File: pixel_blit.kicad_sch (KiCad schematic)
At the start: 42 parts, among them J37 Conn_01x03_Pin, SW1 K2-1808SN-A4SW, U1 RP2350B_C42415655, U10 APS6404L-3SQR-SN, U2 W25Q128JVSIQTR

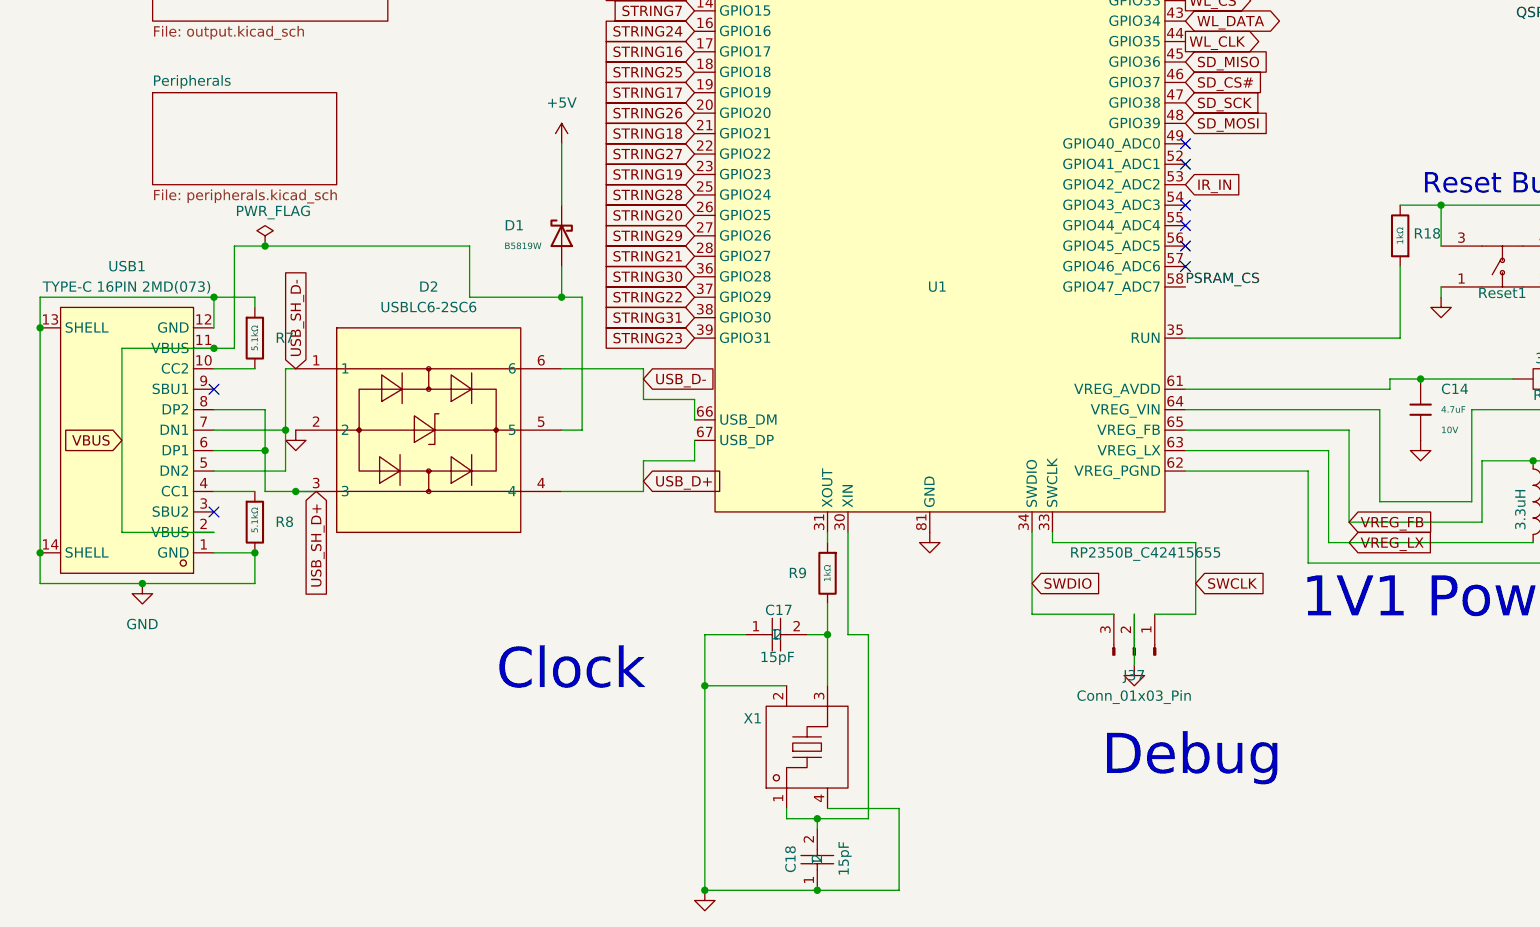
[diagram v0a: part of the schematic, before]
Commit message: Add status RGB LED, user button and blown-fuse LEDs
- D14 common-cathode RGB (C601684) with R72-R74 on GPIO 41/44/45, SW3
  'Play' on GPIO 43; routed from U1 via short F.Cu escapes and In2 lanes
  to the old display area. GPIO 40 and 46 stay spare.
- D15-D18 red LEDs with 10k 0603 across each zone fuse, between holder
  and input terminal.
- Zone borders regenerated; plan doc GPIO map updated.
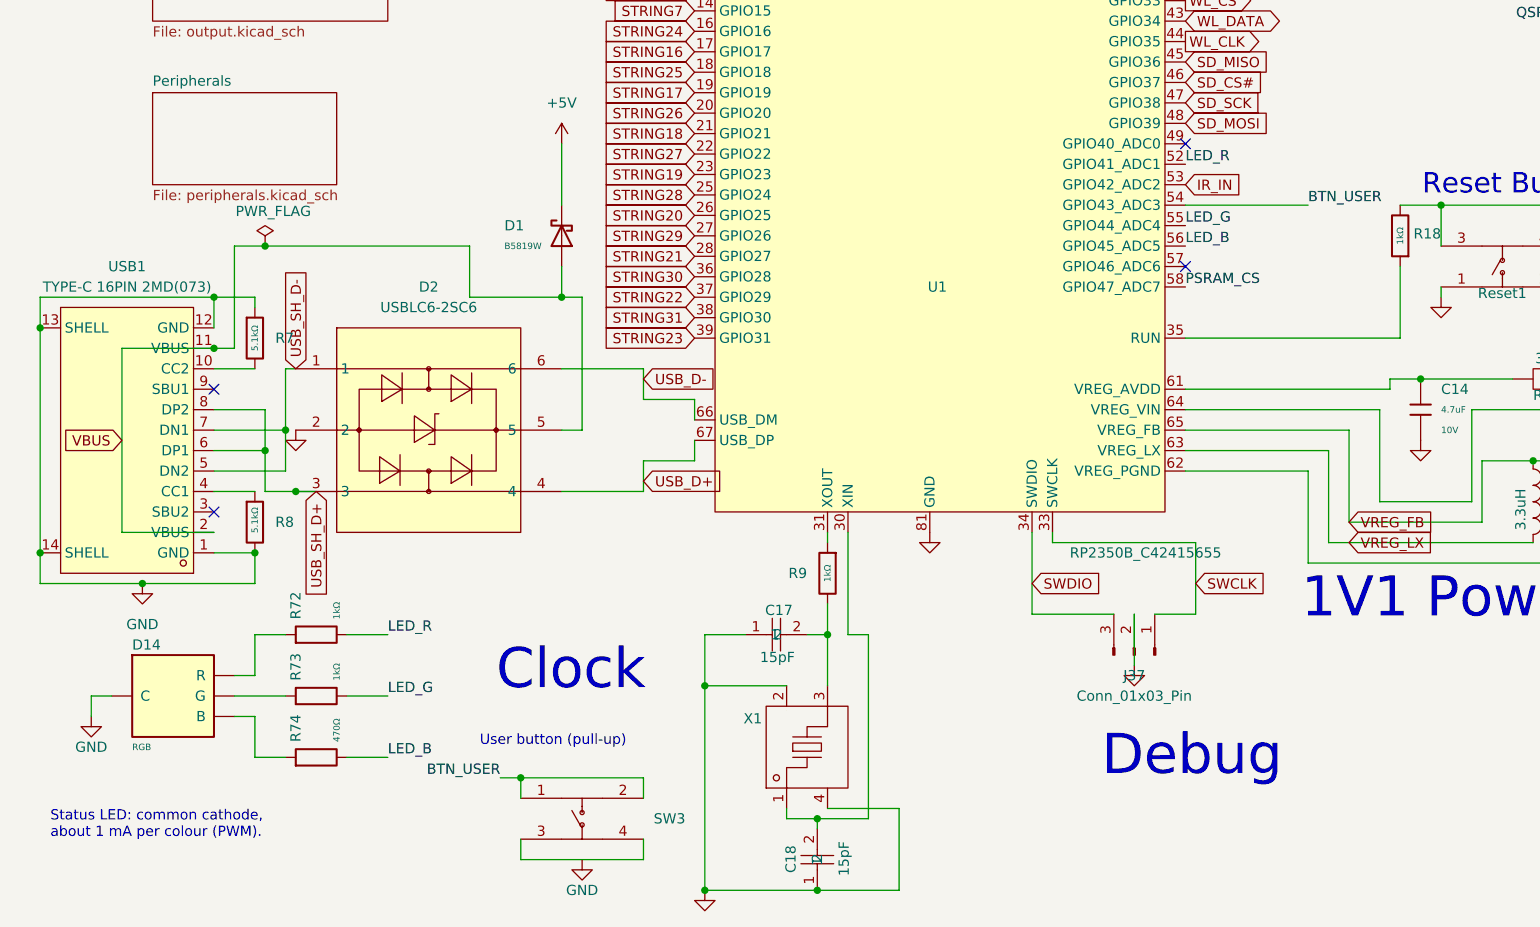
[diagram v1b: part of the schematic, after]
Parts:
- added D14: RGB, JLCImport:TJ-S1615CY6TGLCCSRGB-A5, symbol JLCImport:TJ-S1615CY6TGLCCSRGB-A5
- added R72, R73: 1kΩ, PixelBlit:R_0402, symbol PixelBlit:0402,1kΩ
- added R74: 470Ω, PixelBlit:R_0402, symbol PixelBlit:0402,470Ω
- added SW3: (no value), PixelBlit:KEY-SMD_4P-L4.2-W3.2-P2.20-LS5.1-TL, symbol PixelBlit:K2-1808SN-A4SW
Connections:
- net GND: now also D14.1 (C), SW3.3, SW3.4
- net LED_R: now reaches U1.52 (GPIO41_ADC1)
- net LED_R: now also R72.2
- net BTN_USER: now reaches U1.54 (GPIO43_ADC3)
- net BTN_USER: now also SW3.1, SW3.2
- net LED_G: now reaches U1.55 (GPIO44_ADC4)
- net LED_G: now also R73.2
- net LED_B: now reaches U1.56 (GPIO45_ADC5)
- net LED_B: now also R74.2
- new net: D14.3 (G), R73.1
- new net: D14.2 (B), R74.1
- new net: D14.4 (R), R72.1
- no-connect marks 8 -> 4
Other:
- note added: "Status LED: common cathode, about 1 mA per colour (PWM)."
- note added: "User button (pull-up)"

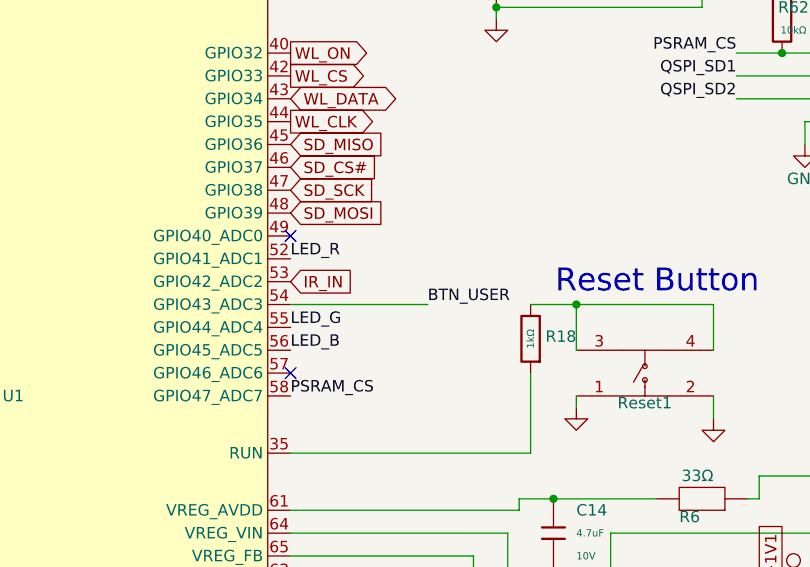
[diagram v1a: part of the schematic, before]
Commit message: Route status LED and button on the old display-panel lines
Replace the In2 lanes with the old TRB/TRA/PSH routes (red GPIO 43,
green GPIO 45, blue GPIO 41) and restore BAK (GPIO 40) for the Play
button. PSH's B.Cu tail moves to F.Cu beside TRB with a short hop under
IR_IN; Boot moves right to clear TRA; RUN via shifted 1 mm.
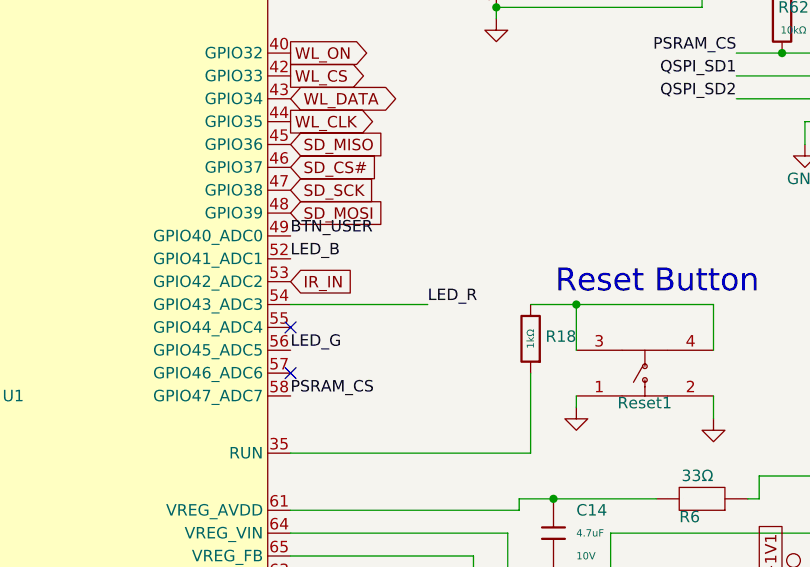
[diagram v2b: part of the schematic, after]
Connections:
- net BTN_USER: now also U1.49 (GPIO40_ADC0); no longer U1.54 (GPIO43_ADC3)
- net LED_B: now also U1.52 (GPIO41_ADC1); no longer U1.56 (GPIO45_ADC5)
- net LED_G: now also U1.56 (GPIO45_ADC5); no longer U1.55 (GPIO44_ADC4)
- net LED_R: now also U1.54 (GPIO43_ADC3); no longer U1.52 (GPIO41_ADC1)

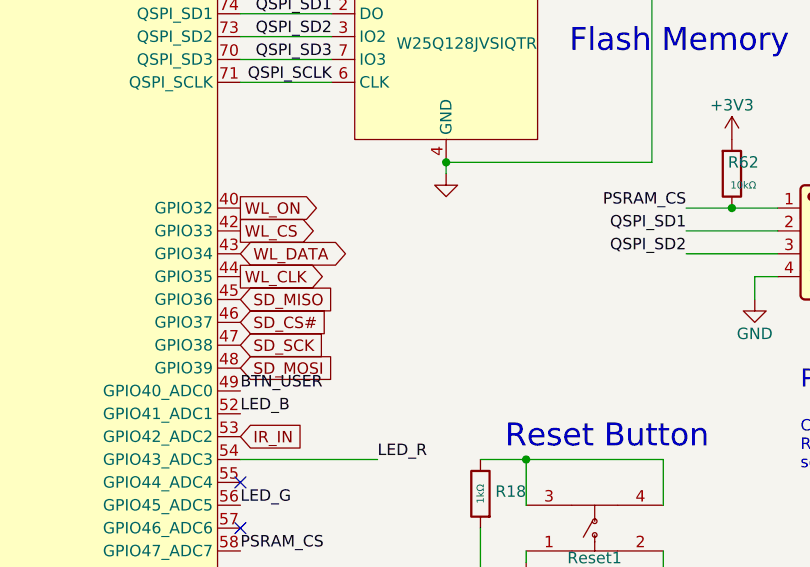
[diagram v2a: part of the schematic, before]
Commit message: Reroute Wi-Fi lanes off SD_MOSI, add 33 ohm series resistor R75 on WL_CLK
The user's In2 reroute shortens the RM2 SPI lines from 147-173 mm to 70-85 mm.
Audit item 2 marked done; README resistor count updated.
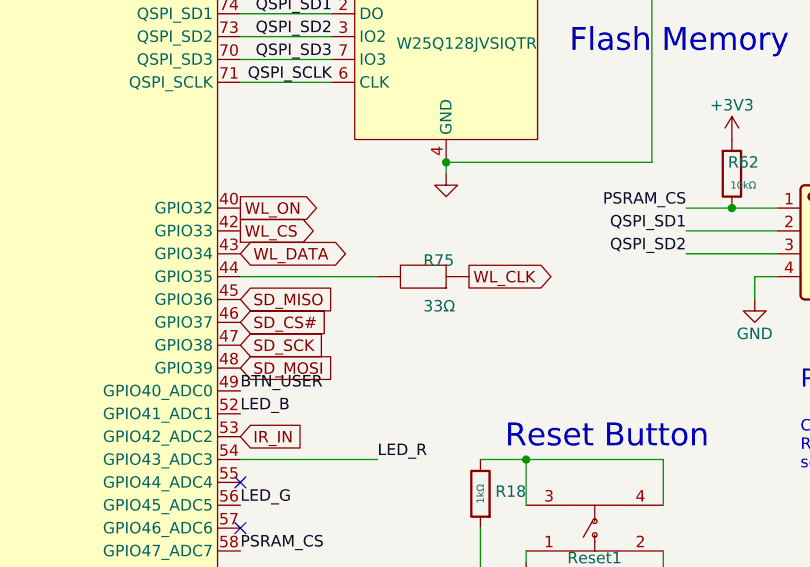
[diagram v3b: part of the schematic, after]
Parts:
- added R75: 33Ω, PixelBlit:R0402, symbol PixelBlit:RT0402BRD0733RL
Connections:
- net WL_CLK: now also R75.1; no longer U1.44 (GPIO35)
- new net: R75.2, U1.44 (GPIO35)
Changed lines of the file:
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@@
 		)
 	)
+	(wire
+		(pts
+			(xy 156.21 88.9) (xy 171.45 88.9)
+		)
+		(stroke
+			(width 0)
+			(type default)
+		)
+	)
 	(global_label "WL_CLK"
 		(shape output)
-		(at 156.21 88.9 0)
+		(at 181.61 88.9 0)
 		(fields_autoplaced yes)
 		(effects
@@
 		)
 		(property "Intersheetrefs" "${INTERSHEET_REFS}"
-			(at 168.3271 88.9 0)
+			(at 193.7271 88.9 0)
 			(hide yes)
 			(show_name no)
@@
 					(unit 1)
 				)
+			)
+		)
+	)
+	(symbol
+		(lib_id "PixelBlit:RT0402BRD0733RL")
+		(at 176.53 88.9 0)
+		(mirror y)
+		(unit 1)
+		(body_style 1)
+		(exclude_from_sim no)
+		(in_bom yes)
+		(on_board yes)
+		(in_pos_files yes)
+		(dnp no)
+		(property "Reference" "R75"
+			(at 176.53 86.36 0)
+			(show_name no)
+			(do_not_autoplace no)
+			(effects
+				(font
+					(size 1.27 1.27)
+				)
+				(justify right top)
+			)
+		)
+		(property "Value" "33Ω"
+			(at 176.53 91.44 0)
+			(show_name no)
+			(do_not_autoplace no)
+			(effects
+				(font
+					(size 1.27 1.27)
+				)
+				(justify right top)
+			)
+		)
+		(property "Footprint" "PixelBlit:R0402"
+			(at 176.53 88.9 0)
+			(hide yes)
+			(show_name no)
+			(do_not_autoplace no)
+			(effects
+				(font
+					(size 1.27 1.27)
+				)
+			)
+		)
+		(property "Datasheet" "https://atta.szlcsc.com/upload/public/pdf/source/20200306/C422600_1E6D84923E4A46A82E41ADD87F860B5C.pdf"
+			(at 176.53 88.9 0)
+			(hide yes)
+			(show_name no)
+			(do_not_autoplace no)
+			(effects
+				(font
+					(size 1.27 1.27)
+				)
+			)
+		)
+		(property "Description" "Type:Thick Film Resistors Resistance:33Ω Tolerance:±1% Tolerance:±1% Power(Watts): Overload Voltage (Max): Temperature Coefficient:±100ppm/℃ Temperature Coefficient:±100ppm/℃ Operating Temperature Range:-55℃~+155℃ Operating Temperature Range:-55℃~+155℃"
+			(at 176.53 88.9 0)
+			(hide yes)
+			(show_name no)
+			(do_not_autoplace no)
+			(effects
+				(font
+					(size 1.27 1.27)
+				)
+				(justify right top)
+			)
+		)
+		(property "Manufacturer Part" "0402WGF330JTCE"
+			(at 176.53 88.9 0)
+			(hide yes)
+			(show_name no)
+			(do_not_autoplace no)
+			(effects
+				(font
+					(size 1.27 1.27)
+				)
+			)
+		)
+		(property "Manufacturer" "UNI-ROYAL(厚声)"
+			(at 176.53 88.9 0)
+			(hide yes)
+			(show_name no)
+			(do_not_autoplace no)
+			(effects
+				(font
+					(size 1.27 1.27)
+				)
+			)
+		)
+		(property "Supplier Part" "C25105"
+			(at 176.53 88.9 0)
+			(hide yes)
+			(show_name no)
+			(do_not_autoplace no)
+			(effects
+				(font
+					(size 1.27 1.27)
+				)
+			)
+		)
+		(property "Supplier" "LCSC"
+			(at 176.53 88.9 0)
+			(hide yes)
+			(show_name no)
+			(do_not_autoplace no)
+			(effects
+				(font
+					(size 1.27 1.27)
+				)
+			)
+		)
+		(property "LCSC Part Name" "33Ω ±1% 62.5mW 厚膜电阻"
+			(at 176.53 88.9 0)
+			(hide yes)
+			(show_name no)
+			(do_not_autoplace no)
+			(effects
+				(font
+					(size 1.27 1.27)
+				)
+			)
+		)
+		(property "LCSC" "C25105"
+			(at 176.53 88.9 0)
+			(hide yes)
+			(show_name no)
+			(do_not_autoplace no)
+			(effects
+				(font
+					(size 1.27 1.27)
+				)
+			)
+		)
+		(pin "1"
+		)
+		(pin "2"
+		)
+		(instances
+			(project "pixel_blit"
+				(path "/046bafbc-5afd-4d51-a157-fe6ddaf6697d"
+					(reference "R75")
+					(unit 1)
+				)
